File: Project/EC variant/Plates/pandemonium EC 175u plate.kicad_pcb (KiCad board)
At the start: 2 copper layers, 199.9 x 81 mm, 38 parts

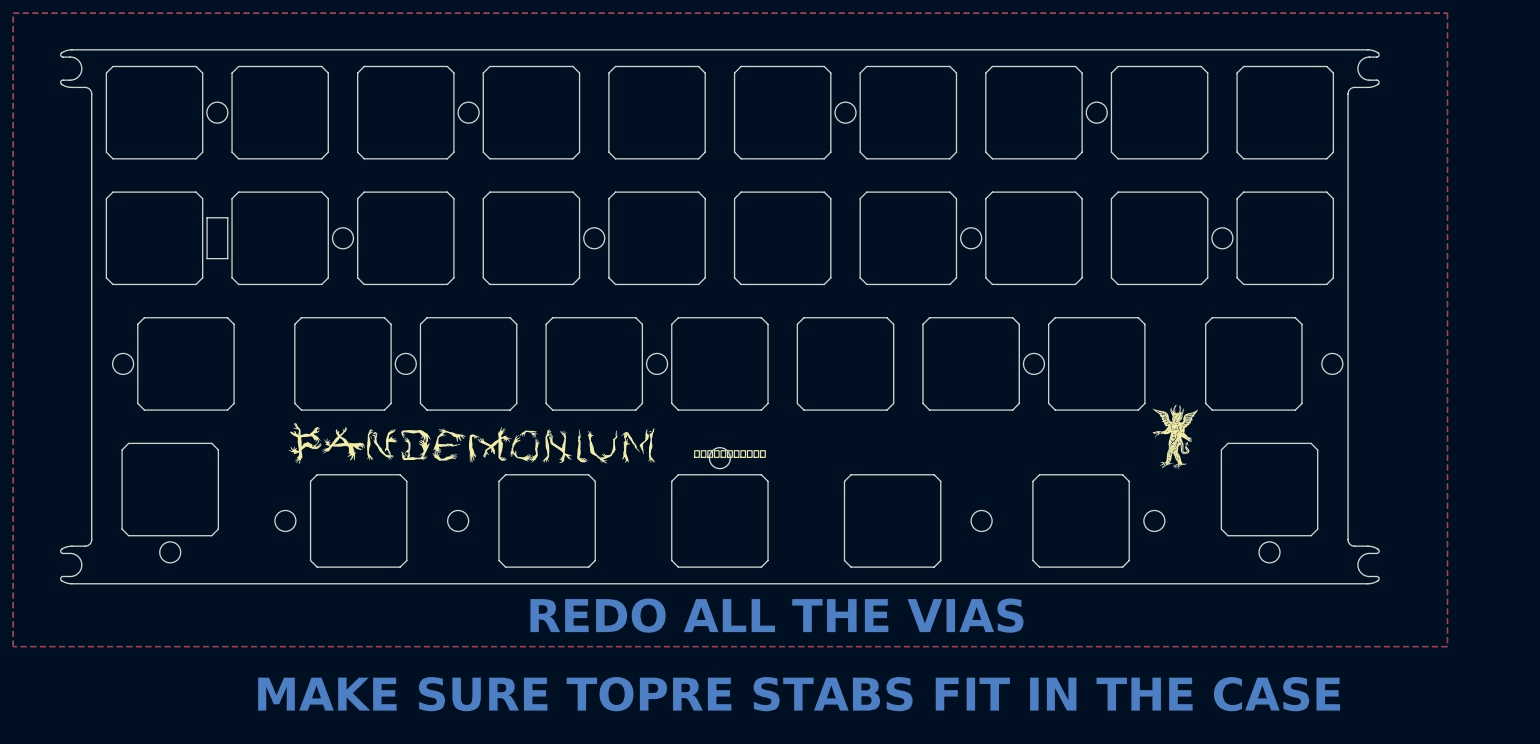
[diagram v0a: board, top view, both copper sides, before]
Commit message: changes to topre version and BLE version
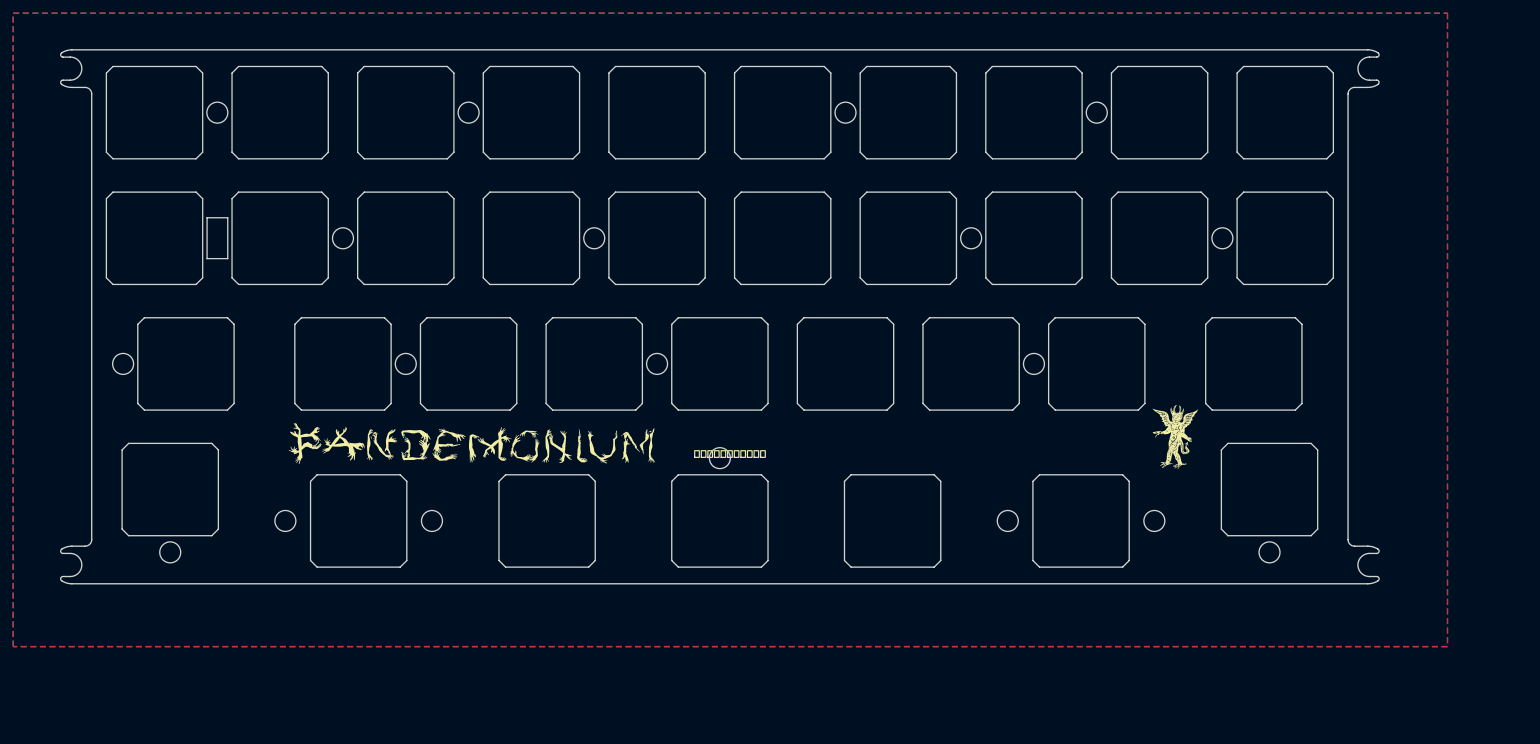
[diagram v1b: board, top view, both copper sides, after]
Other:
- outline, holes or cut-outs redrawn
- board text removed: "MAKE SURE TOPRE STABS FIT IN THE CASE"
- board text removed: "REDO ALL THE VIAS"
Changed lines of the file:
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@@
   (gr_arc (start 225.25 99.075) (mid 226.056102 99.191376) (end 226.796371 99.531)
     (stroke (width 0.2) (type solid)) (layer "Edge.Cuts"))
-  (gr_circle (center 219.86875 71.4375) (end 219.86875 69.85)
-    (stroke (width 0.1) (type default)) (fill none) (layer "Edge.Cuts"))
   (gr_circle (center 61.11875 95.25) (end 61.11875 93.6625)
     (stroke (width 0.1) (type default)) (fill none) (layer "Edge.Cuts"))
@@
   (gr_circle (center 107.95 52.3875) (end 107.95 50.8)
     (stroke (width 0.1) (type default)) (fill none) (layer "Edge.Cuts"))
-  (gr_circle (center 87.3125 95.25) (end 87.3125 93.6625)
+  (gr_circle (center 83.34375 95.25) (end 83.34375 93.6625)
     (stroke (width 0.1) (type default)) (fill none) (layer "Edge.Cuts"))
   (gr_line (start 225.499442 24.9125) (end 226.606464 24.9125)
@@
   (gr_arc (start 226.796369 24.2685) (mid 226.942189 24.661492) (end 226.606464 24.9125)
     (stroke (width 0.2) (type solid)) (layer "Edge.Cuts"))
-  (gr_circle (center 166.6875 95.25) (end 166.6875 93.6625)
+  (gr_circle (center 170.65625 95.25) (end 170.65625 93.6625)
     (stroke (width 0.1) (type default)) (fill none) (layer "Edge.Cuts"))
   (gr_arc (start 226.606464 28.4125) (mid 226.942207 28.663502) (end 226.796369 29.0565)
@@
   (gr_line (start 225.499444 100.175) (end 226.606466 100.175)
     (stroke (width 0.2) (type solid)) (layer "Edge.Cuts"))
-  (gr_text "MAKE SURE TOPRE STABS FIT IN THE CASE" (at 56.35625 124.61875) (layer "B.Cu")
-    (effects (font (size 5 5) (thickness 0.3) bold) (justify left bottom))
-  )
-  (gr_text "REDO ALL THE VIAS" (at 97.63125 112.7125) (layer "B.Cu")
-    (effects (font (size 5 5) (thickness 0.3) bold) (justify left bottom))
-  )
   (gr_text "JLCJLCJLCJLC" (at 127 25.4) (layer "B.SilkS")
     (effects (font (size 1 1) (thickness 0.15)))
